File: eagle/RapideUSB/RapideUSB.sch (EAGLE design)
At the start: 22 parts, among them J1 AVR_SPI_PRG_6PTH, Y1 12-20MHz

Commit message: RapideUSB finished, need final drawings and review before send to production.
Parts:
- added C5: 1uF, resistor:C-EU025-024X044
- added JP1, JP2: M021X02_NO_SILK, SparkFun-Connectors:M021X02_NO_SILK
- added JP3, JP4: M161X16_NO_SILK, SparkFun-Connectors:M161X16_NO_SILK
- added PORTB2313, PORTB328, PORTC, PORTD: (no value), SparkFun-Connectors:M081X08
- added U$2, U$3, U$4, U$5, U$6: M191X19_NO_SILK, SparkFun-Connectors:M191X19_NO_SILK
- JP_D+, JP_D-: value M01PTH -> TEST-POINT3X5; device SparkFun-Connectors:M01PTH -> SparkFun-Passives:TEST-POINT3X5
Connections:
- new net B0: PORTB328.1, UC2.PB0(ICP)
- new net B1: PORTB328.2, UC2.PB1(OC1A)
- new net B2: PORTB328.3, UC2.PB2(SS/OC1B)
- new net B6: C2.2, PORTB328.7, UC1.XTAL1, UC2.PB6(XTAL1/TOSC1), Y1.1
- new net B7: C1.2, PORTB328.8, UC1.XTAL2, UC2.PB7(XTAL2/TOSC2), Y1.2
- new net D0: PORTD.1, UC1.(RXD)PD0, UC2.PD0(RXD)
- new net D1: PORTD.2, UC1.(TXD)PD1, UC2.PD1(TXD)
- new net D2: J_D+D2.1, PORTD.3, UC1.(INT0)PD2, UC2.PD2(INT0)
- new net D3: PORTD.4, UC1.(INT1)PD3, UC2.PD3(INT1)
- new net D4: J_D-D4.1, PORTD.5, UC1.(T0)PD4, UC2.PD4(XCK/T0)
- new net D5: UC1.(T1)PD5
- new net D6: PORTD.7, UC1.(ICP)PD6, UC2.PD6(AIN0)
- new net D7: PORTD.8, UC2.PD7(AIN1)
- new net N$10: PORTC.6, UC2.PC5(ADC5/SCL)
- new net N$11: PORTC.7, UC2.ADC6
- new net N$12: PORTC.8, UC2.ADC7
- new net N$13: PORTB2313.1, UC1.(AIN0)PB0
- new net N$16: PORTD.6, UC2.PD5(T1)
- new net N$5: PORTC.1, UC2.PC0(ADC0)
- new net N$6: PORTC.2, UC2.PC1(ADC1)
- new net N$7: UC2.PC2(ADC2)
- new net N$8: PORTC.4, UC2.PC3(ADC3)
- new net N$9: PORTC.5, UC2.PC4(ADC4/SDA)
- net GND: now also C5.2, JP2.1, JP2.2
- net MISO: now also PORTB2313.7, PORTB328.5
- net MOSI: now also PORTB2313.6, PORTB328.4
- net N$1: now also PORTB2313.5, UC1.PB4; no longer C1.2, UC1.XTAL2, UC2.PB7(XTAL2/TOSC2), Y1.2
- net N$2: now also PORTB2313.4, UC1.(OCI)PB3; no longer C2.2, UC1.XTAL1, UC2.PB6(XTAL1/TOSC1), Y1.1
- net N$3: now also PORTB2313.3, UC1.PB2; no longer J_D-D4.1, UC1.(T0)PD4, UC2.PD4(XCK/T0)
- net N$4: now also PORTB2313.2, UC1.(AIN1)PB1; no longer J_D+D2.1, UC1.(INT0)PD2, UC2.PD2(INT0)
- net SCK: now also PORTB2313.8, PORTB328.6
- net VCC: now also C5.1, JP1.1, JP1.2
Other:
- moved on the sheet: RAIL+, RAIL-

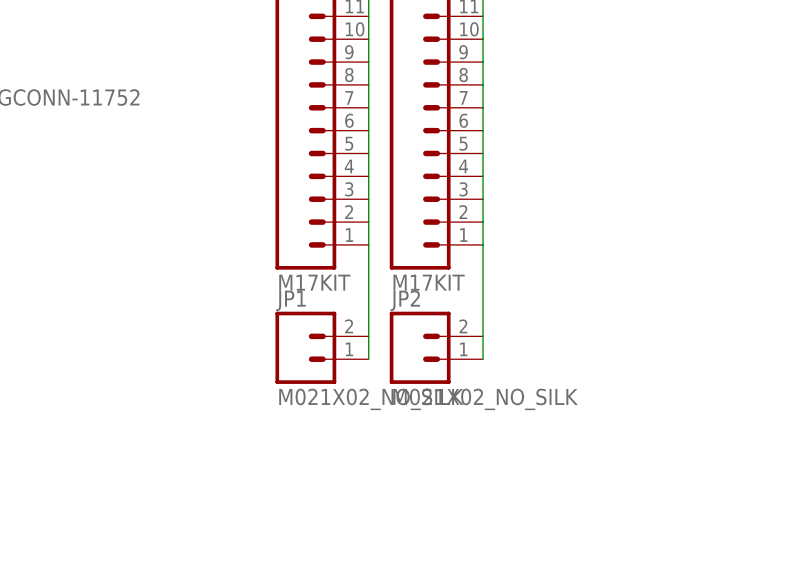
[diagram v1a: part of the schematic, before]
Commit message: v1.1: fixed the power pin top-vias pins and added a nice V-USB logo.
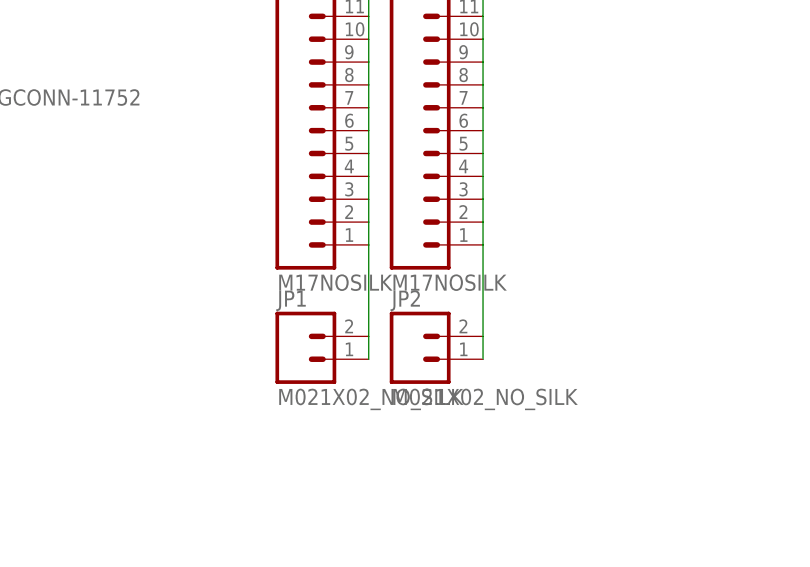
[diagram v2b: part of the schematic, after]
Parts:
- RAIL+, RAIL-: value M17KIT -> M17NOSILK; device SparkFun-Connectors:M17KIT -> SparkFun-Connectors:M17NOSILK
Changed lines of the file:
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@@
 <part name="C3" library="resistor" deviceset="C-EU" device="025-024X044" value="1uF"/>
 <part name="C4" library="resistor" deviceset="CPOL-EU" device="E2-5" value="10uF+"/>
-<part name="RAIL+" library="SparkFun-Connectors" deviceset="M17" device="KIT"/>
-<part name="RAIL-" library="SparkFun-Connectors" deviceset="M17" device="KIT"/>
+<part name="RAIL+" library="SparkFun-Connectors" deviceset="M17" device="NOSILK" value="M17NOSILK"/>
+<part name="RAIL-" library="SparkFun-Connectors" deviceset="M17" device="NOSILK" value="M17NOSILK"/>
 <part name="U$2" library="SparkFun-Connectors" deviceset="M19" device="1X19_NO_SILK"/>
 <part name="U$3" library="SparkFun-Connectors" deviceset="M19" device="1X19_NO_SILK"/>

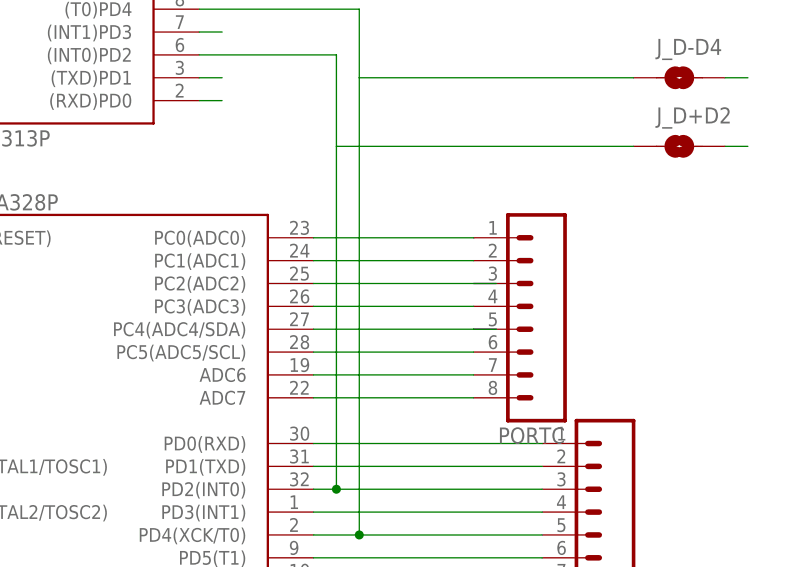
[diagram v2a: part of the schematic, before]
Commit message: I made a mistake and PC2 is in fact not connected
Since I won't make another batch and that routing that one wire looks
like a nightmare, I just remove it from schematics to avoid confusion
later. A good lesson learnt.
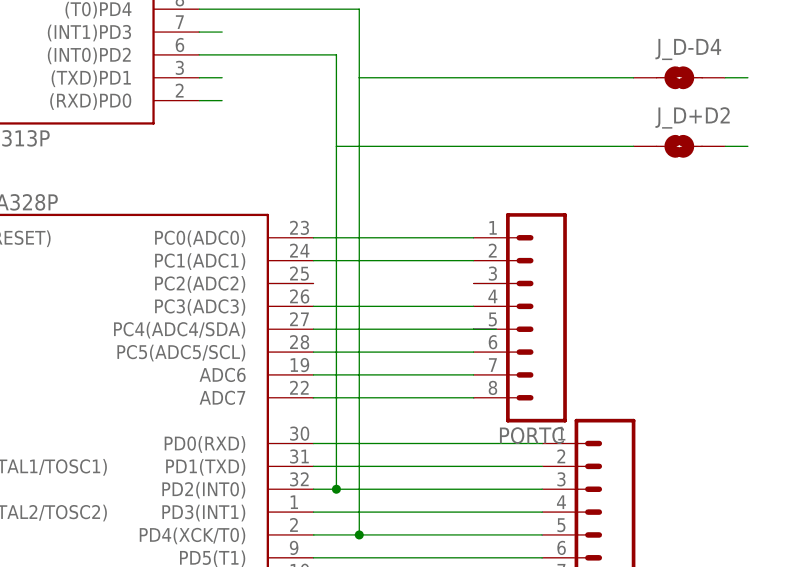
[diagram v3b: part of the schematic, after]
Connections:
- removed net N$7: UC2.PC2(ADC2)
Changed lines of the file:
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@@
 <?xml version="1.0" encoding="utf-8"?>
 <!DOCTYPE eagle SYSTEM "eagle.dtd">
-<eagle version="6.3">
+<eagle version="7.2.0">
 <drawing>
 <settings>
@@
 </segment>
 </net>
-<net name="N$7" class="0">
-<segment>
-<pinref part="UC2" gate="G$1" pin="PC2(ADC2)"/>
-<wire x1="60.96" y1="35.56" x2="81.28" y2="35.56" width="0.1524" layer="91"/>
-</segment>
-</net>

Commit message: Bugfix: PD5 was unconnected on 2313
Added missing wire on board v1.2.
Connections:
- removed net N$16: PORTD.6, UC2.PD5(T1)
- net D5: now also PORTD.6, UC2.PD5(T1)
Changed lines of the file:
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@@
-</segment>
-</net>
-<net name="N$16" class="0">
-<segment>
-<pinref part="UC2" gate="G$1" pin="PD5(T1)"/>
-<pinref part="PORTD" gate="G$1" pin="6"/>
-<wire x1="60.96" y1="5.08" x2="86.36" y2="5.08" width="0.1524" layer="91"/>
 </segment>
 </net>
@@
 <wire x1="48.26" y1="68.58" x2="50.8" y2="68.58" width="0.1524" layer="91"/>
 </segment>
+<segment>
+<pinref part="UC2" gate="G$1" pin="PD5(T1)"/>
+<pinref part="PORTD" gate="G$1" pin="6"/>
+<wire x1="60.96" y1="5.08" x2="86.36" y2="5.08" width="0.1524" layer="91"/>
+</segment>
 </net>

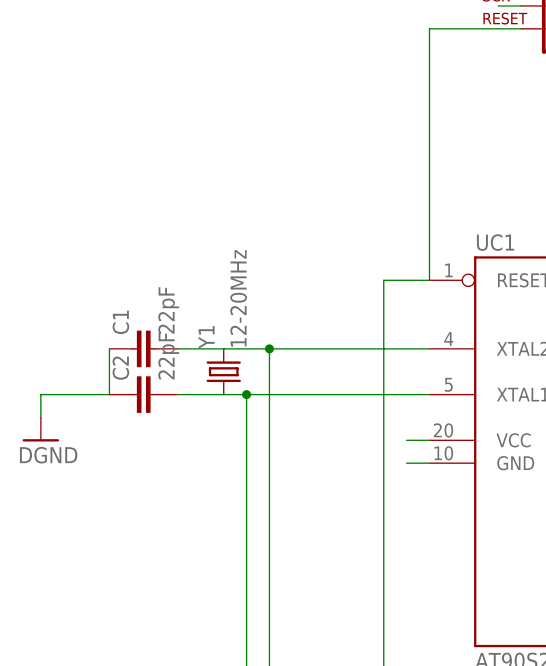
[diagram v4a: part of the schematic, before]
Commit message: Added 2 alternate SMD 22pF caps
That makes 2 airwire because I can't attach to the pad center, but once
made the connection should be all ok.
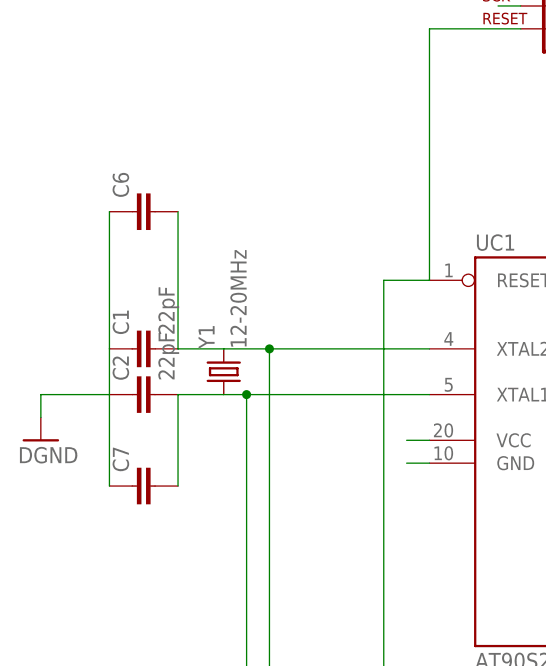
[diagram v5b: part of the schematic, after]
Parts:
- added C6, C7: (no value), resistor:C-EUC1206K
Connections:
- net B6: now also C7.2
- net B7: now also C6.2
- net GND: now also C6.1, C7.1
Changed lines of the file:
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@@
 <part name="JP4" library="SparkFun-Connectors" deviceset="M16" device="1X16_NO_SILK"/>
 <part name="C5" library="resistor" deviceset="C-EU" device="025-024X044" value="1uF"/>
+<part name="C6" library="resistor" deviceset="C-EU" device="C1206K"/>
+<part name="C7" library="resistor" deviceset="C-EU" device="C1206K"/>
 </parts>
 <sheets>
@@
 <instance part="JP4" gate="G$1" x="231.14" y="15.24"/>
 <instance part="C5" gate="G$1" x="119.38" y="38.1"/>
+<instance part="C6" gate="G$1" x="-20.32" y="101.6" rot="R90"/>
+<instance part="C7" gate="G$1" x="-20.32" y="71.12" rot="R90"/>
 </instances>
 <busses>
@@
 <wire x1="-22.86" y1="81.28" x2="-30.48" y2="81.28" width="0.1524" layer="91"/>
 <wire x1="-30.48" y1="81.28" x2="-30.48" y2="78.74" width="0.1524" layer="91"/>
+<pinref part="C6" gate="G$1" pin="1"/>
+<wire x1="-22.86" y1="86.36" x2="-22.86" y2="101.6" width="0.1524" layer="91"/>
+<pinref part="C7" gate="G$1" pin="1"/>
+<wire x1="-22.86" y1="71.12" x2="-22.86" y2="81.28" width="0.1524" layer="91"/>
 </segment>
 <segment>
@@
 <wire x1="2.54" y1="-22.86" x2="78.74" y2="-22.86" width="0.1524" layer="91"/>
 <junction x="2.54" y="10.16"/>
+<pinref part="C6" gate="G$1" pin="2"/>
+<wire x1="-15.24" y1="101.6" x2="-15.24" y2="86.36" width="0.1524" layer="91"/>
 </segment>
 </net>
@@
 <wire x1="5.08" y1="-20.32" x2="78.74" y2="-20.32" width="0.1524" layer="91"/>
 <junction x="5.08" y="15.24"/>
-</segment>
-</net>
+<pinref part="C7" gate="G$1" pin="2"/>
+<wire x1="-15.24" y1="81.28" x2="-15.24" y2="71.12" width="0.1524" layer="91"/>
+</segment>
+</net>
